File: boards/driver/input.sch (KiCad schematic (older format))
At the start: 3 parts, among them Q3 MMBT2222

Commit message: Driver board: a bit more schematic work and some initial footprint selections
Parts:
- R73: footprint Resistor_SMD:R_1206_3216Metric -> Resistor_SMD:R_0603_1608Metric
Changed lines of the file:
@@
 F 0 "R89" V 5145 3350 50  0000 C CNN
 F 1 "500" V 5236 3350 50  0000 C CNN
-F 2 "Resistor_SMD:R_1206_3216Metric" V 5390 3340 50  0001 C CNN
+F 2 "Resistor_SMD:R_0603_1608Metric" V 5390 3340 50  0001 C CNN
 F 3 "~" H 5350 3350 50  0001 C CNN
 	1    5350 3350

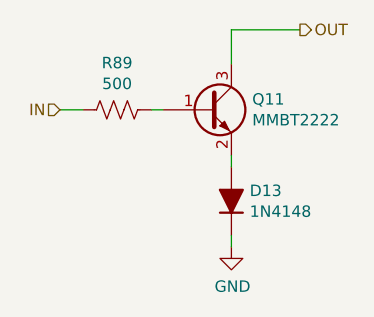
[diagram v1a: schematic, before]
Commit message: Driver board: finished first rough draft schematic. Lots of placeholders, but at least every place is held.
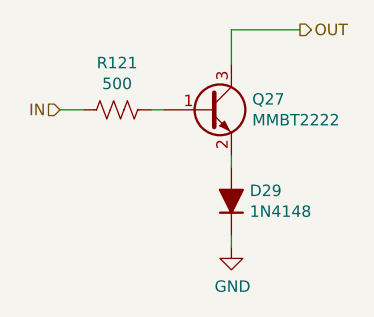
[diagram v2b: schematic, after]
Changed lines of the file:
@@
 $Descr A4 11693 8268
 encoding utf-8
-Sheet 14 68
+Sheet 14 69
 Title ""
 Date ""
@@
 AR Path="/64D2DF1E/618ABD5A/62A099B4" Ref="R117"  Part="1"
 AR Path="/64D2DF1E/618ABD69/62A099B4" Ref="R121"  Part="1"
-F 0 "R89" V 5145 3350 50  0000 C CNN
+F 0 "R121" V 5145 3350 50  0000 C CNN
 F 1 "500" V 5236 3350 50  0000 C CNN
 F 2 "Resistor_SMD:R_0603_1608Metric" V 5390 3340 50  0001 C CNN
@@
 AR Path="/64D2DF1E/618ABD5A/62A099BB" Ref="Q25"  Part="1"
 AR Path="/64D2DF1E/618ABD69/62A099BB" Ref="Q27"  Part="1"
-F 0 "Q11" H 5941 3396 50  0000 L CNN
+F 0 "Q27" H 5941 3396 50  0000 L CNN
 F 1 "MMBT2222" H 5941 3305 50  0000 L CNN
 F 2 "Package_TO_SOT_SMD:SOT-23" H 5950 3450 50  0001 C CNN
@@
 AR Path="/64D2DF1E/618ABD5A/62A09ED6" Ref="D27"  Part="1"
 AR Path="/64D2DF1E/618ABD69/62A09ED6" Ref="D29"  Part="1"
-F 0 "D13" V 5896 3670 50  0000 R CNN
+F 0 "D29" V 5896 3670 50  0000 R CNN
 F 1 "1N4148" V 5805 3670 50  0000 R CNN
 F 2 "Diode_SMD:D_SOD-323" H 5850 3750 50  0001 C CNN

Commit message: Driver board: fleshed out the hotswap controller, tweaked some resistors, and added some bypass caps
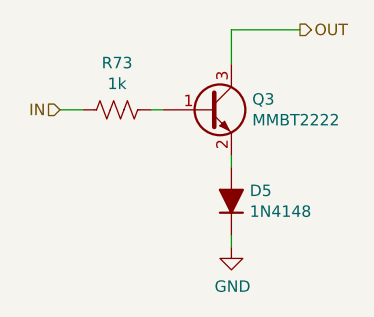
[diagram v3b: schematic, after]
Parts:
- R73: value 500 -> 1k
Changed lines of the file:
@@
 $Descr A4 11693 8268
 encoding utf-8
-Sheet 14 69
+Sheet 6 69
 Title ""
 Date ""
@@
 AR Path="/64D2DF1E/618ABD5A/62A099B4" Ref="R117"  Part="1"
 AR Path="/64D2DF1E/618ABD69/62A099B4" Ref="R121"  Part="1"
-F 0 "R121" V 5145 3350 50  0000 C CNN
-F 1 "500" V 5236 3350 50  0000 C CNN
+F 0 "R73" V 5145 3350 50  0000 C CNN
+F 1 "1k" V 5236 3350 50  0000 C CNN
 F 2 "Resistor_SMD:R_0603_1608Metric" V 5390 3340 50  0001 C CNN
 F 3 "~" H 5350 3350 50  0001 C CNN
@@
 AR Path="/64D2DF1E/618ABD5A/62A099BB" Ref="Q25"  Part="1"
 AR Path="/64D2DF1E/618ABD69/62A099BB" Ref="Q27"  Part="1"
-F 0 "Q27" H 5941 3396 50  0000 L CNN
+F 0 "Q3" H 5941 3396 50  0000 L CNN
 F 1 "MMBT2222" H 5941 3305 50  0000 L CNN
 F 2 "Package_TO_SOT_SMD:SOT-23" H 5950 3450 50  0001 C CNN
@@
 AR Path="/64D2DF1E/618ABD5A/62A09ED6" Ref="D27"  Part="1"
 AR Path="/64D2DF1E/618ABD69/62A09ED6" Ref="D29"  Part="1"
-F 0 "D29" V 5896 3670 50  0000 R CNN
+F 0 "D5" V 5896 3670 50  0000 R CNN
 F 1 "1N4148" V 5805 3670 50  0000 R CNN
 F 2 "Diode_SMD:D_SOD-323" H 5850 3750 50  0001 C CNN
@@
 	5850 3900 5850 3950
 $Comp
-L power:GND #PWR037
+L power:GND #PWR040
 U 1 1 62A0A585
 P 5850 3950
-AR Path="/64D2DF1E/62A081E6/62A0A585" Ref="#PWR037"  Part="1"
-AR Path="/64D2DF1E/61899537/62A0A585" Ref="#PWR039"  Part="1"
-AR Path="/64D2DF1E/6189F17F/62A0A585" Ref="#PWR041"  Part="1"
-AR Path="/64D2DF1E/618A1433/62A0A585" Ref="#PWR043"  Part="1"
-AR Path="/64D2DF1E/618A1442/62A0A585" Ref="#PWR045"  Part="1"
-AR Path="/64D2DF1E/618A404F/62A0A585" Ref="#PWR047"  Part="1"
-AR Path="/64D2DF1E/618A405E/62A0A585" Ref="#PWR049"  Part="1"
-AR Path="/64D2DF1E/618A406D/62A0A585" Ref="#PWR051"  Part="1"
-AR Path="/64D2DF1E/618A407C/62A0A585" Ref="#PWR053"  Part="1"
-AR Path="/64D2DF1E/618ABD3C/62A0A585" Ref="#PWR055"  Part="1"
-AR Path="/64D2DF1E/618ABD4B/62A0A585" Ref="#PWR057"  Part="1"
-AR Path="/64D2DF1E/618ABD5A/62A0A585" Ref="#PWR059"  Part="1"
-AR Path="/64D2DF1E/618ABD69/62A0A585" Ref="#PWR061"  Part="1"
-F 0 "#PWR061" H 5850 3700 50  0001 C CNN
+AR Path="/64D2DF1E/62A081E6/62A0A585" Ref="#PWR040"  Part="1"
+AR Path="/64D2DF1E/61899537/62A0A585" Ref="#PWR042"  Part="1"
+AR Path="/64D2DF1E/6189F17F/62A0A585" Ref="#PWR044"  Part="1"
+AR Path="/64D2DF1E/618A1433/62A0A585" Ref="#PWR046"  Part="1"
+AR Path="/64D2DF1E/618A1442/62A0A585" Ref="#PWR048"  Part="1"
+AR Path="/64D2DF1E/618A404F/62A0A585" Ref="#PWR050"  Part="1"
+AR Path="/64D2DF1E/618A405E/62A0A585" Ref="#PWR052"  Part="1"
+AR Path="/64D2DF1E/618A406D/62A0A585" Ref="#PWR054"  Part="1"
+AR Path="/64D2DF1E/618A407C/62A0A585" Ref="#PWR056"  Part="1"
+AR Path="/64D2DF1E/618ABD3C/62A0A585" Ref="#PWR058"  Part="1"
+AR Path="/64D2DF1E/618ABD4B/62A0A585" Ref="#PWR060"  Part="1"
+AR Path="/64D2DF1E/618ABD5A/62A0A585" Ref="#PWR062"  Part="1"
+AR Path="/64D2DF1E/618ABD69/62A0A585" Ref="#PWR064"  Part="1"
+F 0 "#PWR040" H 5850 3700 50  0001 C CNN
 F 1 "GND" H 5855 3777 50  0000 C CNN
 F 2 "" H 5850 3950 50  0001 C CNN
